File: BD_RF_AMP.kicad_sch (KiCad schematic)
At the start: 35 parts, among them Q2301 2SC3357, T2301 XFMR_RF_BIFILAR, U2301 AS169-73, U2302 AS169-73

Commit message: Update pcb database to version 6
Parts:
- C2301, C2302, C2303, C2304, C2309, C2310, C2311, C2312, C2314, C2315: symbol Custom:C_US -> custom:C_US; PartNumber 800238-104 -> 800063-XXX
- C2305, C2306, C2307, C2308: symbol Custom:C_US -> custom:C_US; PartNumber 800238-102 -> 800063-XXX
- C2313: symbol Custom:C_US_0805_0.1UF_X7R_10%_50V_HS -> custom:C_US_0805_0.1UF_X7R_10%_50V_HS; PartNumber 800239-151 -> 800238-104
- E2301, E2302, E2303: symbol Custom:FB0805 -> custom:FB0805; PartNumber 800245-601 -> 80000X-XXX
- L2301: symbol Custom:L_US -> custom:L_US; PartNumber 800YYY-YYY -> 8000XX-XXX
- Q2301: symbol Custom:2SC3357 -> custom:2SC3357
- R2301, R2302: symbol Custom:R_US -> custom:R_US; PartNumber 800235-000 -> 800XXX-XXX
- R2303, R2304: symbol Custom:R_US -> custom:R_US; PartNumber 800235-330 -> 800XXX-XXX
- R2305: symbol Custom:R_US -> custom:R_US; PartNumber 800235-202 -> 800XXX-XXX
- R2306: symbol Custom:R_US -> custom:R_US; PartNumber 800235-360 -> 800XXX-XXX
- R2307, R2308: symbol Custom:R_US -> custom:R_US; PartNumber 800235-151 -> 800XXX-XXX
- R2309: symbol Custom:R_US -> custom:R_US; PartNumber 800235-331 -> 800XXX-XXX
- R2310: symbol Custom:R_US -> custom:R_US; PartNumber 800235-361 -> 800XXX-XXX
- R2311: symbol Custom:R_US -> custom:R_US; PartNumber 800235-220 -> 800XXX-XXX
- R2312: symbol Custom:R_US -> custom:R_US; PartNumber 800235-300 -> 800XXX-XXX
- T2301: symbol Custom:XFMR_RF_BIFILAR -> custom:XFMR_RF_BIFILAR
- U2301, U2302: symbol Custom:AS169-73 -> custom:AS169-73

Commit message: Fix BOM part number errors and out of sync footprints which happened during conversion from Kicad 5 to 6
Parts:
- C2301, C2302, C2303, C2304, C2309, C2310, C2311, C2312, C2314, C2315: PartNumber 800063-XXX -> 800238-104
- C2305, C2306, C2307, C2308: PartNumber 800063-XXX -> 800239-103
- C2313: PartNumber 800238-104 -> 800239-151
- E2301, E2302, E2303: PartNumber 80000X-XXX -> 800245-601
- R2301, R2302: PartNumber 800XXX-XXX -> 800235-000
- R2303, R2304: PartNumber 800XXX-XXX -> 800235-330
- R2305: PartNumber 800XXX-XXX -> 800235-202
- R2306: PartNumber 800XXX-XXX -> 800235-360
- R2307, R2308: PartNumber 800XXX-XXX -> 800235-151
- R2309: PartNumber 800XXX-XXX -> 800235-331
- R2310: PartNumber 800XXX-XXX -> 800235-361
- R2311: PartNumber 800XXX-XXX -> 800235-220
- R2312: PartNumber 800XXX-XXX -> 800235-300
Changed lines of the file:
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@@
       (effects (font (size 1.524 1.524)))
     )
-    (property "PartNumber" "800XXX-XXX" (id 4) (at 132.08 127.762 90)
+    (property "PartNumber" "800235-331" (id 4) (at 132.08 127.762 90)
       (effects (font (size 1.524 1.524)) hide)
     )
@@
       (effects (font (size 1.524 1.524)))
     )
-    (property "PartNumber" "800XXX-XXX" (id 4) (at 144.272 152.4 90)
+    (property "PartNumber" "800235-300" (id 4) (at 144.272 152.4 90)
       (effects (font (size 1.524 1.524)) hide)
     )
@@
       (effects (font (size 1.524 1.524)))
     )
-    (property "PartNumber" "800XXX-XXX" (id 4) (at 122.682 152.4 90)
+    (property "PartNumber" "800235-220" (id 4) (at 122.682 152.4 90)
       (effects (font (size 1.524 1.524)) hide)
     )
@@
       (effects (font (size 1.524 1.524)))
     )
-    (property "PartNumber" "800XXX-XXX" (id 4) (at 102.362 107.95 90)
+    (property "PartNumber" "800235-202" (id 4) (at 102.362 107.95 90)
       (effects (font (size 1.524 1.524)) hide)
     )
@@
       (effects (font (size 1.524 1.524)))
     )
-    (property "PartNumber" "800XXX-XXX" (id 4) (at 219.202 130.81 90)
+    (property "PartNumber" "800235-151" (id 4) (at 219.202 130.81 90)
       (effects (font (size 1.524 1.524)) hide)
     )
@@
       (effects (font (size 1.524 1.524)))
     )
-    (property "PartNumber" "800XXX-XXX" (id 4) (at 238.252 130.81 90)
+    (property "PartNumber" "800235-151" (id 4) (at 238.252 130.81 90)
       (effects (font (size 1.524 1.524)) hide)
     )
@@
       (effects (font (size 1.524 1.524)))
     )
-    (property "PartNumber" "800XXX-XXX" (id 4) (at 226.06 117.602 90)
+    (property "PartNumber" "800235-360" (id 4) (at 226.06 117.602 90)
       (effects (font (size 1.524 1.524)) hide)
     )
@@
       (effects (font (size 1.524 1.524)))
     )
-    (property "PartNumber" "800XXX-XXX" (id 4) (at 102.362 152.4 90)
+    (property "PartNumber" "800235-361" (id 4) (at 102.362 152.4 90)
       (effects (font (size 1.524 1.524)) hide)
     )
@@
       (effects (font (size 1.524 1.524)))
     )
-    (property "PartNumber" "80000X-XXX" (id 4) (at 66.675 94.615 0)
+    (property "PartNumber" "800245-601" (id 4) (at 66.675 94.615 0)
       (effects (font (size 1.524 1.524)) hide)
     )
@@
       (effects (font (size 1.524 1.524)))
     )
-    (property "PartNumber" "800063-XXX" (id 4) (at 53.34 95.25 0)
+    (property "PartNumber" "800238-104" (id 4) (at 53.34 95.25 0)
       (effects (font (size 1.524 1.524)) hide)
     )
@@
       (effects (font (size 1.524 1.524)))
     )
-    (property "PartNumber" "800063-XXX" (id 4) (at 50.8 74.93 0)
+    (property "PartNumber" "800238-104" (id 4) (at 50.8 74.93 0)
       (effects (font (size 1.524 1.524)) hide)
     )
@@
       (effects (font (size 1.524 1.524)))
     )
-    (property "PartNumber" "80000X-XXX" (id 4) (at 172.085 83.185 0)
+    (property "PartNumber" "800245-601" (id 4) (at 172.085 83.185 0)
       (effects (font (size 1.524 1.524)) hide)
     )
@@
       (effects (font (size 1.524 1.524)))
     )
-    (property "PartNumber" "80000X-XXX" (id 4) (at 193.675 86.995 0)
+    (property "PartNumber" "800245-601" (id 4) (at 193.675 86.995 0)
       (effects (font (size 1.524 1.524)) hide)
     )
@@
       (effects (font (size 1.524 1.524)))
     )
-    (property "PartNumber" "800063-XXX" (id 4) (at 77.47 93.98 0)
+    (property "PartNumber" "800239-103" (id 4) (at 77.47 93.98 0)
       (effects (font (size 1.524 1.524)) hide)
     )
@@
       (effects (font (size 1.524 1.524)))
     )
-    (property "PartNumber" "800XXX-XXX" (id 4) (at 39.37 93.472 90)
+    (property "PartNumber" "800235-330" (id 4) (at 39.37 93.472 90)
       (effects (font (size 1.524 1.524)) hide)
     )
@@
       (effects (font (size 1.524 1.524)))
     )
-    (property "PartNumber" "800XXX-XXX" (id 4) (at 39.37 97.282 90)
+    (property "PartNumber" "800235-330" (id 4) (at 39.37 97.282 90)
       (effects (font (size 1.524 1.524)) hide)
     )
@@
       (effects (font (size 1.524 1.524)))
     )
-    (property "PartNumber" "800063-XXX" (id 4) (at 88.9 93.98 0)
+    (property "PartNumber" "800239-103" (id 4) (at 88.9 93.98 0)
       (effects (font (size 1.524 1.524)) hide)
     )
@@
       (effects (font (size 1.524 1.524)))
     )
-    (property "PartNumber" "800063-XXX" (id 4) (at 215.9 86.36 0)
+    (property "PartNumber" "800239-103" (id 4) (at 215.9 86.36 0)
       (effects (font (size 1.524 1.524)) hide)
     )
@@
       (effects (font (size 1.524 1.524)))
     )
-    (property "PartNumber" "800063-XXX" (id 4) (at 240.03 86.36 0)
+    (property "PartNumber" "800239-103" (id 4) (at 240.03 86.36 0)
       (effects (font (size 1.524 1.524)) hide)
     )
@@
       (effects (font (size 1.524 1.524)))
     )
-    (property "PartNumber" "800XXX-XXX" (id 4) (at 22.86 79.502 90)
+    (property "PartNumber" "800235-000" (id 4) (at 22.86 79.502 90)
       (effects (font (size 1.524 1.524)) hide)
     )
@@
       (effects (font (size 1.524 1.524)))
     )
-    (property "PartNumber" "800XXX-XXX" (id 4) (at 276.86 79.502 90)
+    (property "PartNumber" "800235-000" (id 4) (at 276.86 79.502 90)
       (effects (font (size 1.524 1.524)) hide)
     )
@@
       (effects (font (size 1.524 1.524)))
     )
-    (property "PartNumber" "800063-XXX" (id 4) (at 133.35 54.61 0)
+    (property "PartNumber" "800238-104" (id 4) (at 133.35 54.61 0)
       (effects (font (size 1.524 1.524)) hide)
     )
@@
       (effects (font (size 1.524 1.524)))
     )
-    (property "PartNumber" "800063-XXX" (id 4) (at 262.89 74.93 0)
+    (property "PartNumber" "800238-104" (id 4) (at 262.89 74.93 0)
       (effects (font (size 1.524 1.524)) hide)
     )
@@
       (effects (font (size 1.524 1.524)))
     )
-    (property "PartNumber" "800063-XXX" (id 4) (at 220.98 113.03 0)
+    (property "PartNumber" "800238-104" (id 4) (at 220.98 113.03 0)
       (effects (font (size 1.524 1.524)) hide)
     )
@@
       (effects (font (size 1.524 1.524)))
     )
-    (property "PartNumber" "800063-XXX" (id 4) (at 123.19 123.19 0)
+    (property "PartNumber" "800238-104" (id 4) (at 123.19 123.19 0)
       (effects (font (size 1.524 1.524)) hide)
     )
@@
       (effects (font (size 1.524 1.524)))
     )
-    (property "PartNumber" "800063-XXX" (id 4) (at 100.33 130.81 0)
+    (property "PartNumber" "800238-104" (id 4) (at 100.33 130.81 0)
       (effects (font (size 1.524 1.524)) hide)
     )
@@
       (effects (font (size 1.524 1.524)))
     )
-    (property "PartNumber" "800063-XXX" (id 4) (at 143.51 147.32 0)
+    (property "PartNumber" "800238-104" (id 4) (at 143.51 147.32 0)
       (effects (font (size 1.524 1.524)) hide)
     )
@@
       (effects (font (size 1.524 1.524)))
     )
-    (property "PartNumber" "800238-104" (id 4) (at 245.11 110.49 0)
+    (property "PartNumber" "800239-151" (id 4) (at 245.11 110.49 0)
       (effects (font (size 1.524 1.524)) hide)
     )
@@
       (effects (font (size 1.524 1.524)))
     )
-    (property "PartNumber" "800063-XXX" (id 4) (at 142.24 95.25 0)
+    (property "PartNumber" "800238-104" (id 4) (at 142.24 95.25 0)
       (effects (font (size 1.524 1.524)) hide)
     )
@@
       (effects (font (size 1.524 1.524)))
     )
-    (property "PartNumber" "800063-XXX" (id 4) (at 118.11 78.74 0)
-      (effects (font (size 1.524 1.524)) hide)
-    )
+    (property "PartNumber" "800238-104" (id 4) (at 118.11 78.74 0)
+      (effects (font (size 1.524 1.524)) hide)
+    )

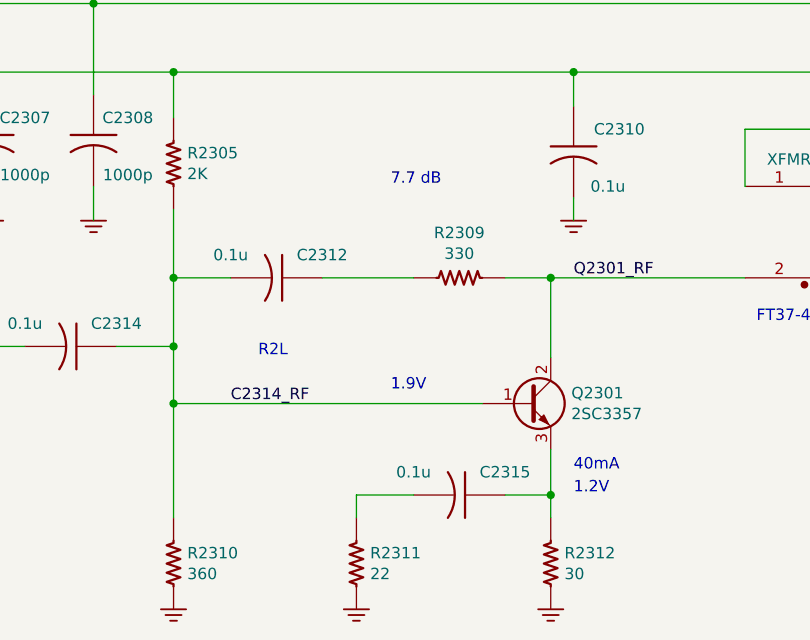
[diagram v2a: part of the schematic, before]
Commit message: Change bias resistors on 2SC3357 amplifiers to stay under 12V across Vbe.
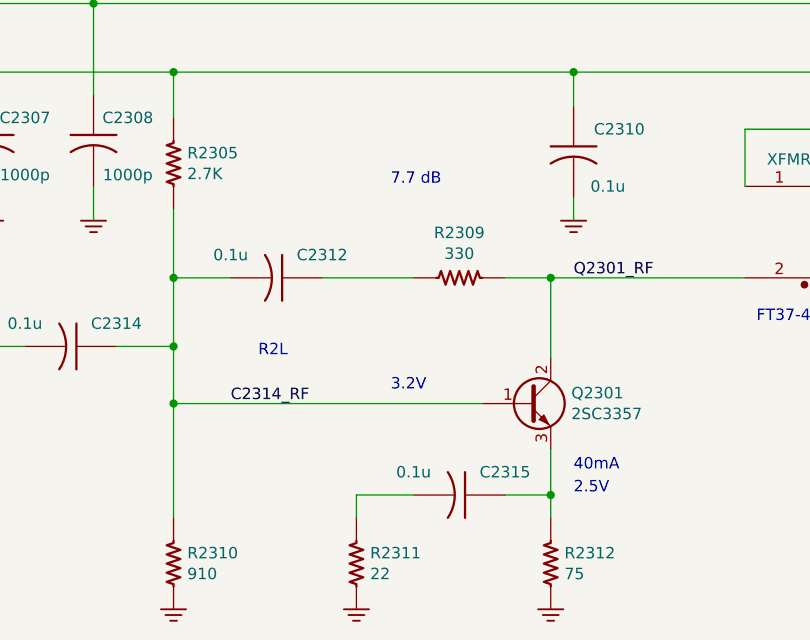
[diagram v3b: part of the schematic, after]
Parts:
- R2305: value 2K -> 2.7K; PartNumber 800235-202 -> 800235-272
- R2310: value 360 -> 910; PartNumber 800235-361 -> 800235-911
- R2312: value 30 -> 75; PartNumber 800235-300 -> 800235-750
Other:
- note added: "2.5V"
- note added: "3.2V"
- note removed: "1.2V"
- note removed: "1.9V"
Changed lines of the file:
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@@
     (effects (font (size 1.27 1.27)) (justify right bottom))
   )
-  (text "1.9V\n" (at 121.92 135.89 0)
+  (text "3.2V\n" (at 121.92 135.89 0)
     (effects (font (size 1.27 1.27)) (justify left bottom))
   )
@@
     (effects (font (size 1.27 1.27)) (justify left bottom))
   )
-  (text "1.2V" (at 142.24 147.32 0)
+  (text "2.5V" (at 142.24 147.32 0)
     (effects (font (size 1.27 1.27)) (justify left bottom))
   )
@@
       (effects (font (size 1.27 1.27)) (justify left))
     )
-    (property "Value" "30" (id 1) (at 141.224 156.083 0)
+    (property "Value" "75" (id 1) (at 141.224 156.083 0)
       (effects (font (size 1.27 1.27)) (justify left))
     )
@@
       (effects (font (size 1.524 1.524)))
     )
-    (property "PartNumber" "800235-300" (id 4) (at 144.272 152.4 90)
+    (property "PartNumber" "800235-750" (id 4) (at 144.272 152.4 90)
       (effects (font (size 1.524 1.524)) hide)
     )
@@
       (effects (font (size 1.27 1.27)) (justify left))
     )
-    (property "Value" "2K" (id 1) (at 99.314 111.633 0)
+    (property "Value" "2.7K" (id 1) (at 99.314 111.633 0)
       (effects (font (size 1.27 1.27)) (justify left))
     )
@@
       (effects (font (size 1.524 1.524)))
     )
-    (property "PartNumber" "800235-202" (id 4) (at 102.362 107.95 90)
+    (property "PartNumber" "800235-272" (id 4) (at 102.362 107.95 90)
       (effects (font (size 1.524 1.524)) hide)
     )
@@
       (effects (font (size 1.27 1.27)) (justify left))
     )
-    (property "Value" "360" (id 1) (at 99.314 156.083 0)
+    (property "Value" "910" (id 1) (at 99.314 156.083 0)
       (effects (font (size 1.27 1.27)) (justify left))
     )
@@
       (effects (font (size 1.524 1.524)))
     )
-    (property "PartNumber" "800235-361" (id 4) (at 102.362 152.4 90)
-      (effects (font (size 1.524 1.524)) hide)
-    )
+    (property "PartNumber" "800235-911" (id 4) (at 102.362 152.4 90)
+      (effects (font (size 1.524 1.524)) hide)
+    )

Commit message: trx_mobo_concept_2_B. Change design to use a dedicated 8V supply for the 2SC3357 parts. Add S-Meter connector. Change mic connector to 3 pins and add 8V sopower supply to pin 3.
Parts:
- C1201: renamed from C2301; value 0.1u -> (none); footprint Capacitor_SMD:C_0805_2012Metric_Pad1.15x1.40mm_HandSolder -> (none)
- C1202: renamed from C2302; value 0.1u -> (none); footprint Capacitor_SMD:C_0805_2012Metric_Pad1.15x1.40mm_HandSolder -> (none)
- C1203: renamed from C2303; value 0.1u -> (none); footprint Capacitor_SMD:C_0805_2012Metric_Pad1.15x1.40mm_HandSolder -> (none)
- C1204: renamed from C2304; value 0.1u -> (none); footprint Capacitor_SMD:C_0805_2012Metric_Pad1.15x1.40mm_HandSolder -> (none)
- C1205: renamed from C2305; value 1000p -> (none); footprint Capacitor_SMD:C_0805_2012Metric_Pad1.15x1.40mm_HandSolder -> (none); PartNumber 800239-103 -> 800239-102
- C1206: renamed from C2306; value 1000p -> (none); footprint Capacitor_SMD:C_0805_2012Metric_Pad1.15x1.40mm_HandSolder -> (none); PartNumber 800239-103 -> 800239-102
- C1207: renamed from C2307; value 1000p -> (none); footprint Capacitor_SMD:C_0805_2012Metric_Pad1.15x1.40mm_HandSolder -> (none); PartNumber 800239-103 -> 800239-102
- C1208: renamed from C2308; value 1000p -> (none); footprint Capacitor_SMD:C_0805_2012Metric_Pad1.15x1.40mm_HandSolder -> (none); PartNumber 800239-103 -> 800239-102
- C1209: renamed from C2309; value 0.1u -> (none); footprint Capacitor_SMD:C_0805_2012Metric_Pad1.15x1.40mm_HandSolder -> (none)
- C1210: renamed from C2310; value 0.1u -> (none); footprint Capacitor_SMD:C_0805_2012Metric_Pad1.15x1.40mm_HandSolder -> (none)
- C1211: renamed from C2311; value 0.1u -> (none); footprint Capacitor_SMD:C_0805_2012Metric_Pad1.15x1.40mm_HandSolder -> (none)
- C1212: renamed from C2312; value 0.1u -> (none); footprint Capacitor_SMD:C_0805_2012Metric_Pad1.15x1.40mm_HandSolder -> (none)
- C1213: renamed from C2313; value 150p -> (none); footprint Capacitor_SMD:C_0805_2012Metric_Pad1.15x1.40mm_HandSolder -> (none)
- C1214: renamed from C2314; value 0.1u -> (none); footprint Capacitor_SMD:C_0805_2012Metric_Pad1.15x1.40mm_HandSolder -> (none)
- C1215: renamed from C2315; value 0.1u -> (none); footprint Capacitor_SMD:C_0805_2012Metric_Pad1.15x1.40mm_HandSolder -> (none)
- E1201: renamed from E2301; value FB0805 -> (none); footprint Inductor_SMD:L_0805_2012Metric_Pad1.15x1.40mm_HandSolder -> (none)
- E1202: renamed from E2302; value FB0805 -> (none); footprint Inductor_SMD:L_0805_2012Metric_Pad1.15x1.40mm_HandSolder -> (none)
- E1203: renamed from E2303; value FB0805 -> (none); footprint Inductor_SMD:L_0805_2012Metric_Pad1.15x1.40mm_HandSolder -> (none)
- L1201: renamed from L2301; value 81nH -> (none); footprint mods:AIR_CORE_9MMX6.3MM -> (none); PartNumber 8000XX-XXX -> 8XXXXX-XXX
- Q1201: renamed from Q2301; value 2SC3357 -> (none); footprint Package_TO_SOT_SMD:SOT-89-3 -> (none)
- R1201: renamed from R2301; value 0 -> (none); footprint Resistor_SMD:R_0805_2012Metric_Pad1.15x1.40mm_HandSolder -> (none)
- R1202: renamed from R2302; value 0 -> (none); footprint Resistor_SMD:R_0805_2012Metric_Pad1.15x1.40mm_HandSolder -> (none)
- R1203: renamed from R2303; value 33 -> (none); footprint Resistor_SMD:R_0805_2012Metric_Pad1.15x1.40mm_HandSolder -> (none)
- R1204: renamed from R2304; value 33 -> (none); footprint Resistor_SMD:R_0805_2012Metric_Pad1.15x1.40mm_HandSolder -> (none)
- R1205: renamed from R2305; value 2.7K -> (none); footprint Resistor_SMD:R_0805_2012Metric_Pad1.15x1.40mm_HandSolder -> (none); PartNumber 800235-272 -> 800235-112
- R1206: renamed from R2306; value 36 -> (none); footprint Resistor_SMD:R_0805_2012Metric_Pad1.15x1.40mm_HandSolder -> (none)
- R1207: renamed from R2309; value 330 -> (none); footprint Resistor_SMD:R_0805_2012Metric_Pad1.15x1.40mm_HandSolder -> (none); PartNumber 800235-331 -> 800235-911
- R1208: renamed from R2307; value 150 -> (none); footprint Resistor_SMD:R_0805_2012Metric_Pad1.15x1.40mm_HandSolder -> (none)
- R1209: renamed from R2308; value 150 -> (none); footprint Resistor_SMD:R_0805_2012Metric_Pad1.15x1.40mm_HandSolder -> (none)
- R1210: renamed from R2310; value 910 -> (none); footprint Resistor_SMD:R_0805_2012Metric_Pad1.15x1.40mm_HandSolder -> (none); PartNumber 800235-911 -> 800235-361
- R1211: renamed from R2311; value 22 -> (none); footprint Resistor_SMD:R_0805_2012Metric_Pad1.15x1.40mm_HandSolder -> (none); PartNumber 800235-220 -> 800235-100
- R1212: renamed from R2312; value 75 -> (none); footprint Resistor_SMD:R_0805_2012Metric_Pad1.15x1.40mm_HandSolder -> (none); PartNumber 800235-750 -> 800235-300
- T1201: renamed from T2301; value XFMR_RF_BIFILAR -> (none); footprint mods:XFMR_Handwound_FT37 -> (none)
- U1201: renamed from U2301; value AS169-73 -> (none); footprint Package_TO_SOT_SMD:SOT-23-6_Handsoldering -> (none)
- U1202: renamed from U2302; value AS169-73 -> (none); footprint Package_TO_SOT_SMD:SOT-23-6_Handsoldering -> (none)
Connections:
- net P13V8_R2L renamed P8V0_R2L
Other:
- note added: "1.2V"
- note added: "1.9V"
- note added: "16.8dB"
- note added: "FT37-43: 10T #30 AWG BIFILAR"
- note added: "HANDWOUND 20 AWG/ 0.8mm bus wire 5T 0.25 in. /6.35mm drill bit 0.375 in/9 mm length Wire length 6in./15cm."
- note removed: "2.5V"
- note removed: "3.2V"
- note removed: "7.7 dB"
- note removed: "FT37-43: 10T BIFILAR"
- note removed: "HANDWOUND 20 AWG/ 0.8mm enamel 5T 0.25 in. /6.35mm drill bit 0.375 in/9 mm length Wire length 6in./15cm. Strip 0.6 in/1.5cm of insulation from each end"
